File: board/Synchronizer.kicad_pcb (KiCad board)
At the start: 2 copper layers, 99 x 62 mm, 52 parts, among them J1 POWER, J2 Conn_01x14, J3 SENSE COIL, J4 Barrel_Jack_Switch, J5 DRIVE COIL, Q1 2N3904, Q2 2N3906, Q3 IRF9540N, Q4 2N3904, U1 Pico, U2 LM7805_TO220, U3 LM358

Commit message: Add R22/C10 snubber across the drive FET drain
R22 (10R) and C10 (100 nF) in series from the Q3 drain node to ground,
damping the ringing when the P-channel FET switches the drive coil off.
They sit on the junction between Q3's drain and R6, so the snubber sees the
switching node itself rather than the coil terminal, which already has D2
across it.

Schematic gains R22, C10, #PWR026 and the wiring to reach them; the PCB
gains their footprints and the new Net-(C10-Pad2).

D2, J5 and R18 shifted a few millimetres to open up room in the drive-coil
corner, and U2 moved slightly. No other footprint changed position, nothing
was removed, and the board is still single-sided with no vias.

Regenerated from the edited design: gerbers, drill files, the schematic PDF,
the board render, and the footprint info cache. Most of the diff in the
.kicad_pcb is the refilled copper zones rather than anything logical.

Co-Authored-By: Claude Opus 5 <noreply@anthropic.com>
Claude-Session: https://claude.ai/code/session_01AQX6646joaK2TkbMXHZigW
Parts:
- added C10: 100 nF, Capacitor_THT:C_Rect_L7.0mm_W2.5mm_P5.00mm, F.Cu at (57.9, 49.8)
- added R22: 10R, Resistor_THT:R_Axial_DIN0207_L6.3mm_D2.5mm_P7.62mm_Horizontal, F.Cu at (54.6, 52.8)
- moved J5 4.74 mm to (67.6, 55.4)
- moved R18 3.75 mm to (76.5, 51.3)
- moved D2 3.37 mm to (72.6, 51.6)
- moved U2 0.68 mm to (37.8, 42.8)
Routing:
- net GND: track 412.8 -> 422.3 mm
- net Net-(Q3-D): track 13.1 -> 19.1 mm
- net Net-(C10-Pad2): track 0.00 -> 4.11 mm
- net Net-(D2-K): track 21.1 -> 18.5 mm
- net +12V: track 94.9 -> 93.7 mm
- added copper zone on F.Cu, net GND
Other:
- board text added: "CLOCK SYNCHRONIZER CIRCUIT BY DL MARKS, CC-BY-SA 4.0 VERSION 1"
- board text removed: "COIL"

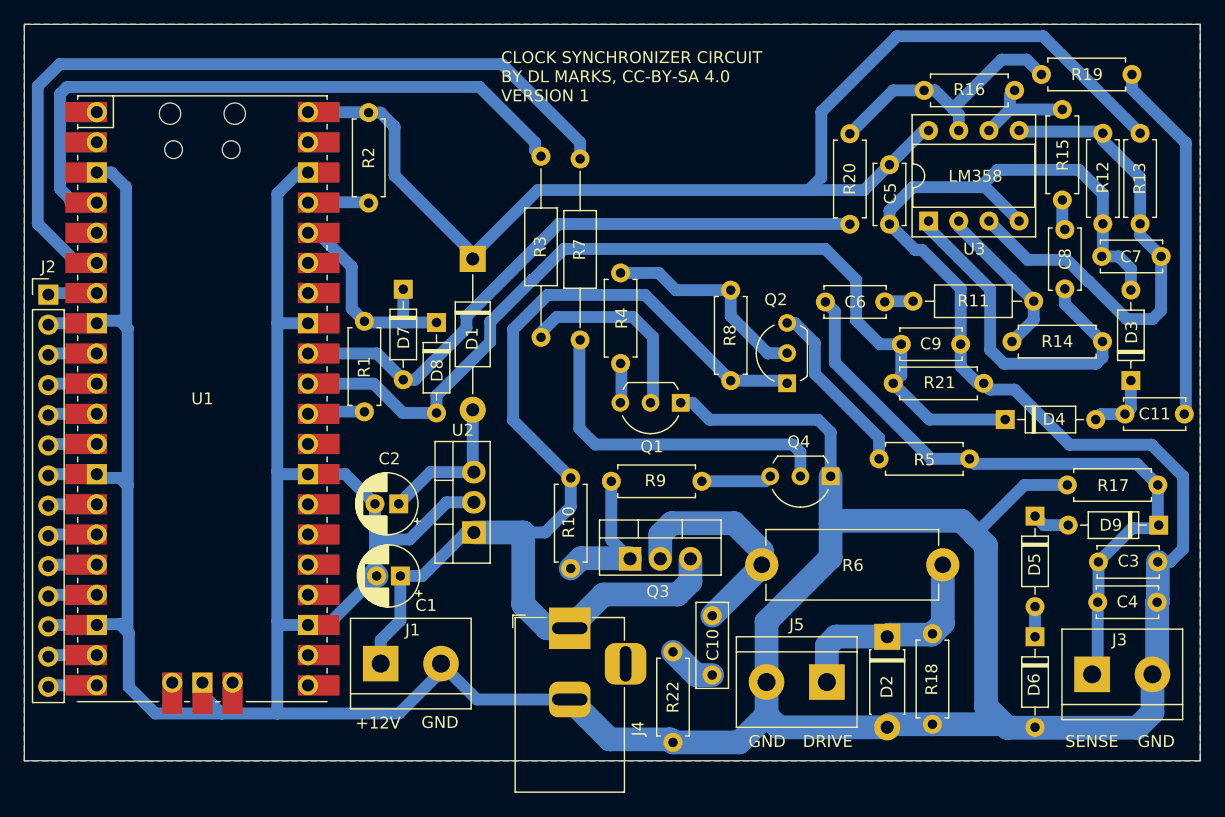
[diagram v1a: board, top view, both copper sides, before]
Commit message: board/CAD: schematic and PCB revisions, add coil bobbin model
board/: schematic and PCB updates (new connector and polarized cap, power
rail reworked in places), regenerated gerbers/drill files, updated
schematic PDF and board render.

CAD/: revise WeightedElectromagnetHolder, add CoilBobbin (model + STL).

Co-Authored-By: Claude Sonnet 5 <noreply@anthropic.com>
Claude-Session: https://claude.ai/code/session_01AQX6646joaK2TkbMXHZigW
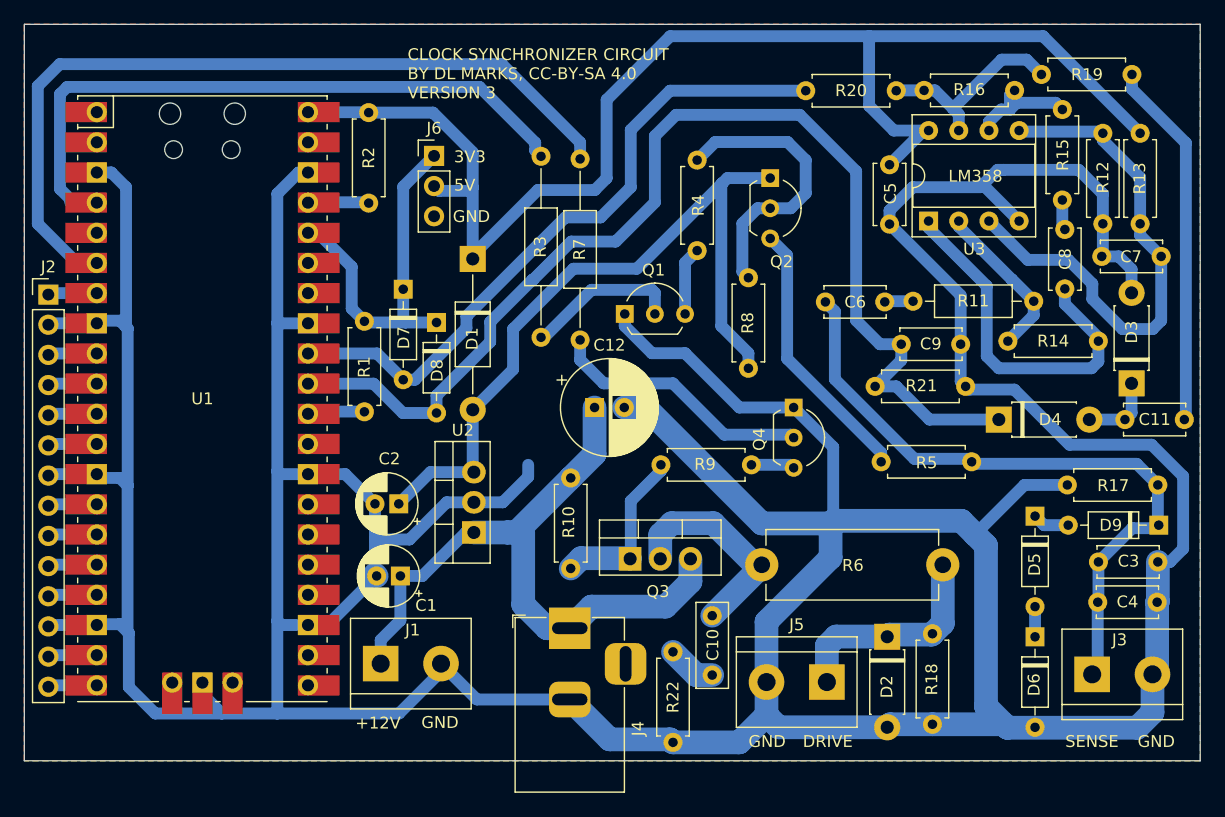
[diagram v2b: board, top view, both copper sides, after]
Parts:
- added C12: 1000 uF, Capacitor_THT:CP_Radial_D8.0mm_P2.50mm, F.Cu at (48.0, 32.3)
- added J6: Conn_01x03, Connector_PinHeader_2.54mm:PinHeader_1x03_P2.54mm_Vertical, F.Cu at (34.5, 11.1)
- C6: value 100 pF -> 30 pF
- D3, D4: value 1N4148 -> 1N5819; footprint Diode_THT:D_DO-35_SOD27_P7.62mm_Horizontal -> Diode_THT:D_DO-41_SOD81_P7.62mm_Horizontal
- R10, R8: value 100k -> 10k
- R14: value 100k -> 33k
- R19: value 10k -> 330R
- R5: value 10k -> 100k
- R9: value 10k -> 1k
- moved Q2 17.3 mm to (62.8, 12.9), turned to -90 degrees
- moved R4 11.5 mm to (56.6, 11.4)
- moved Q1 8.84 mm to (50.5, 24.4), turned to 0 degrees
- moved Q4 6.57 mm to (64.8, 32.3), turned to -90 degrees
- moved R20 5.33 mm to (73.4, 5.59), turned to 180 degrees
- moved R9 4.40 mm to (53.6, 37.1)
- moved R8 1.82 mm to (61.0, 29.0)
- moved R21 1.55 mm to (71.6, 30.5)
- moved D4 0.54 mm to (82.0, 33.3)
- moved C11 0.46 mm to (97.7, 33.3)
- moved R14 0.35 mm to (90.4, 26.7)
- moved R5 0.31 mm to (72.1, 36.8)
- moved D3 0.24 mm to (93.2, 30.2)
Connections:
- net Net-(D7-K) renamed +3V3
- Q2 pad 1: +12V -> +5V
- R8 pad 1: +12V -> +5V
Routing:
- net +5V: track 12.7 -> 64.5 mm
- net GND: track 422.3 -> 459.1 mm
- net +12V: track 93.7 -> 58.5 mm
- net /AMPLITUDE: track 78.1 -> 97.9 mm
- net +3V3: track 19.0 -> 31.3 mm
- net OPSUPPLY: track 104.6 -> 115.4 mm
- net Net-(Q2-C): track 15.0 -> 22.7 mm
- net Net-(Q4-B): track 28.9 -> 22.4 mm
- net Net-(Q2-B): track 18.1 -> 24.4 mm
- net Net-(R16-Pad1): track 22.6 -> 17.2 mm
- net /OSC_SIGNAL: track 52.6 -> 56.3 mm
- net Net-(Q1-B): track 16.7 -> 13.1 mm
- net Net-(Q1-C): track 3.38 -> 5.75 mm
- net Net-(Q4-C): track 5.93 -> 3.66 mm
- net Net-(U3A-+): track 42.3 -> 44.3 mm
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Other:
- board text added: "3V3"
- board text added: "5V"
- board text added: "CLOCK SYNCHRONIZER CIRCUIT BY DL MARKS, CC-BY-SA 4.0 VERSION 3"
- board text removed: "CLOCK SYNCHRONIZER CIRCUIT BY DL MARKS, CC-BY-SA 4.0 VERSION 1"
